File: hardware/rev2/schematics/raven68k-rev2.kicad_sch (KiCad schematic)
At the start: 16 parts, among them J1 CPLD_JTAG, SW1 RESET_SW, U1 MCP100-465D, U2 68010D, U3 XC9572XL-TQ100, X1 CLOCK

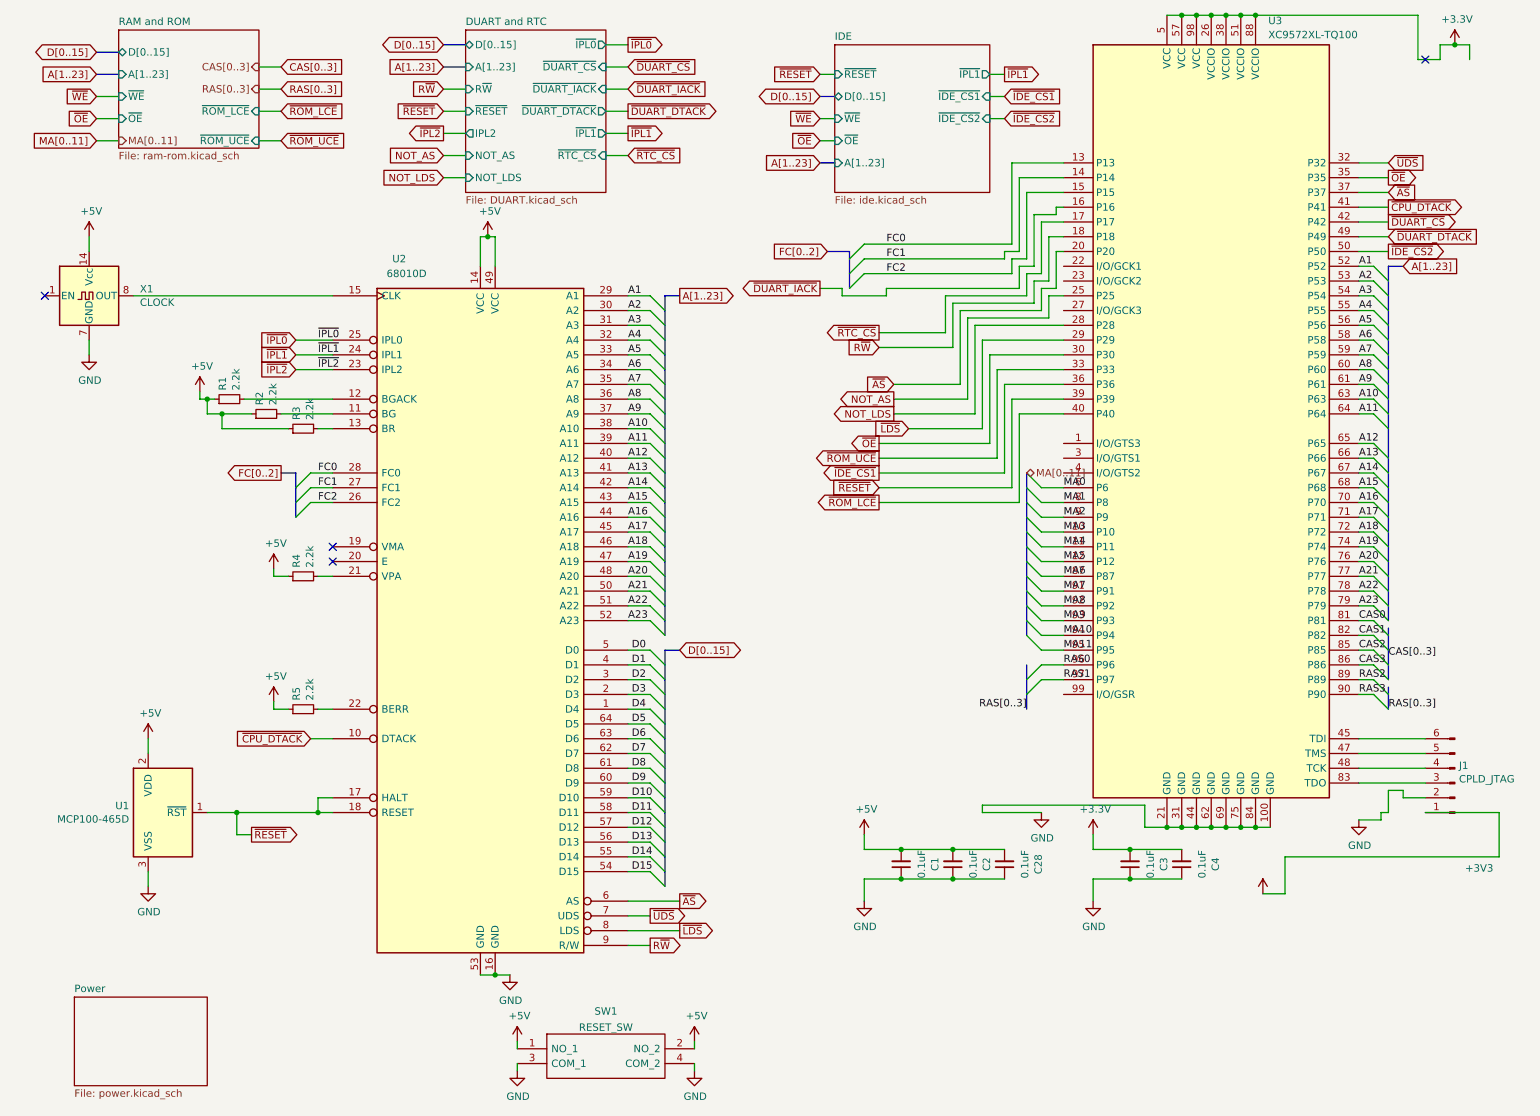
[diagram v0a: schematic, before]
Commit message: Minor adjustment to add the CLK signal to the CPLD that was forgotten. Re-did the PCB to reflect this change and also edited the component placement a bit.
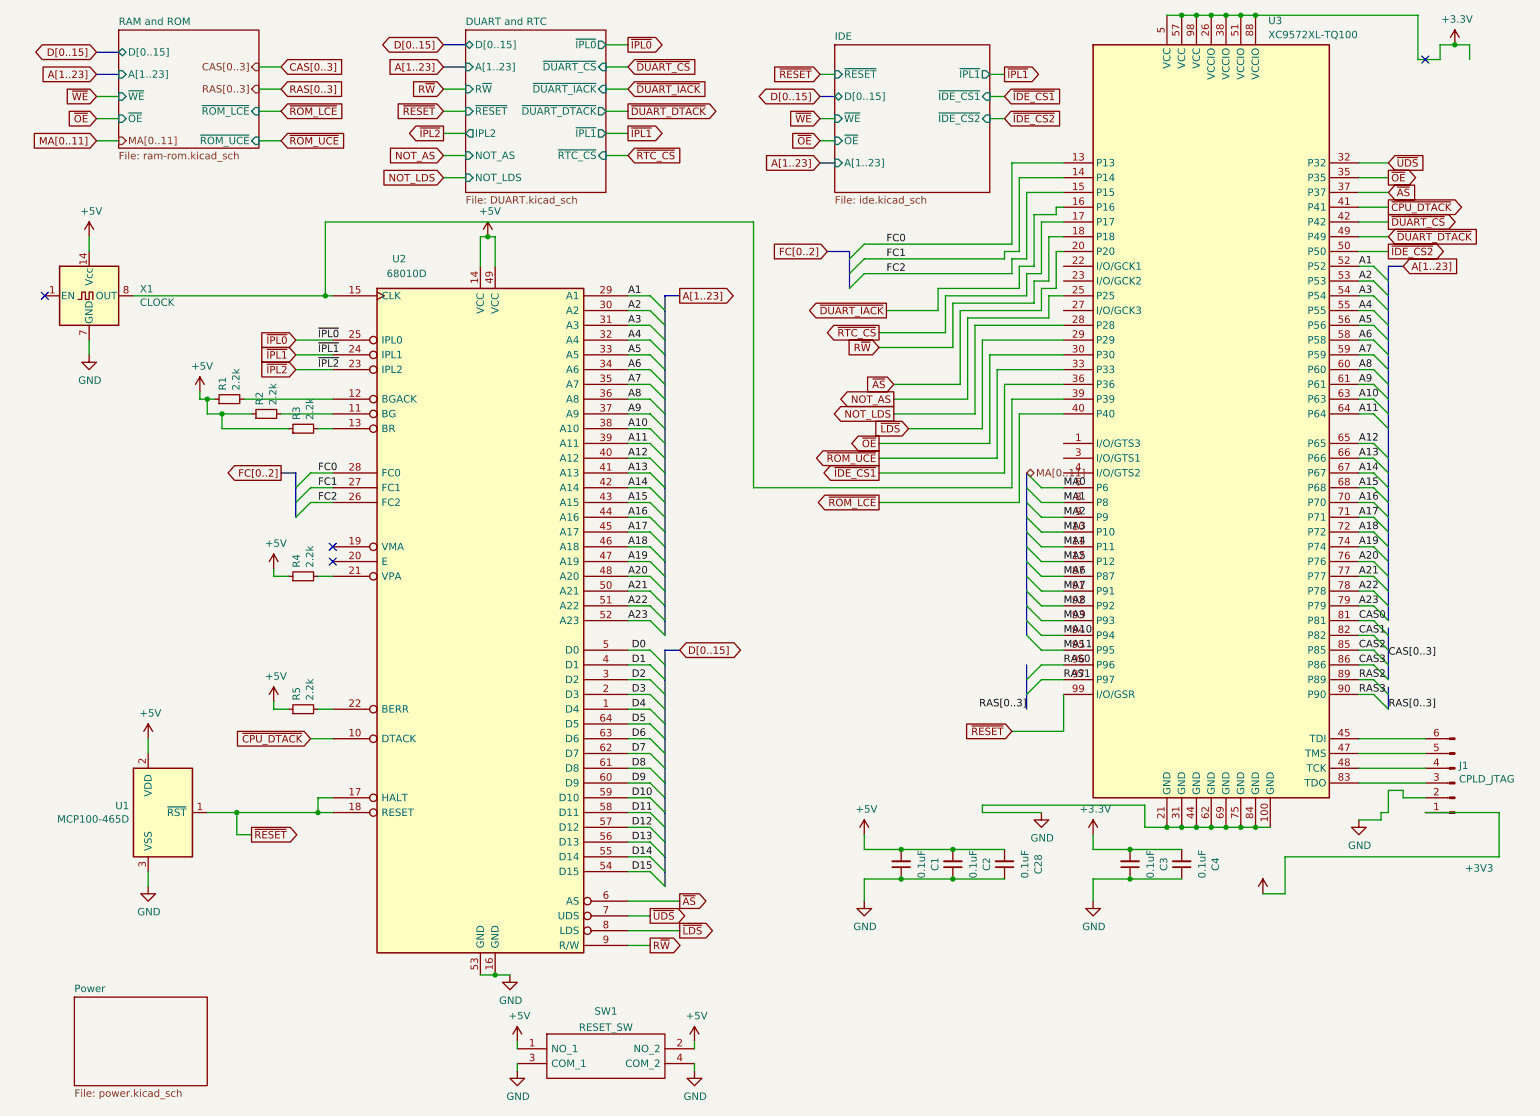
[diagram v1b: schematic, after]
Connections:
- net ~{RESET}: now also U3.99 (I/O/GSR); no longer U3.39 (P39)
- net at U2.15 (CLK), X1.8 (OUT): now also U3.39 (P39)

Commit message: ERC fixes, part 1
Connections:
- no-connect marks 4 -> 10

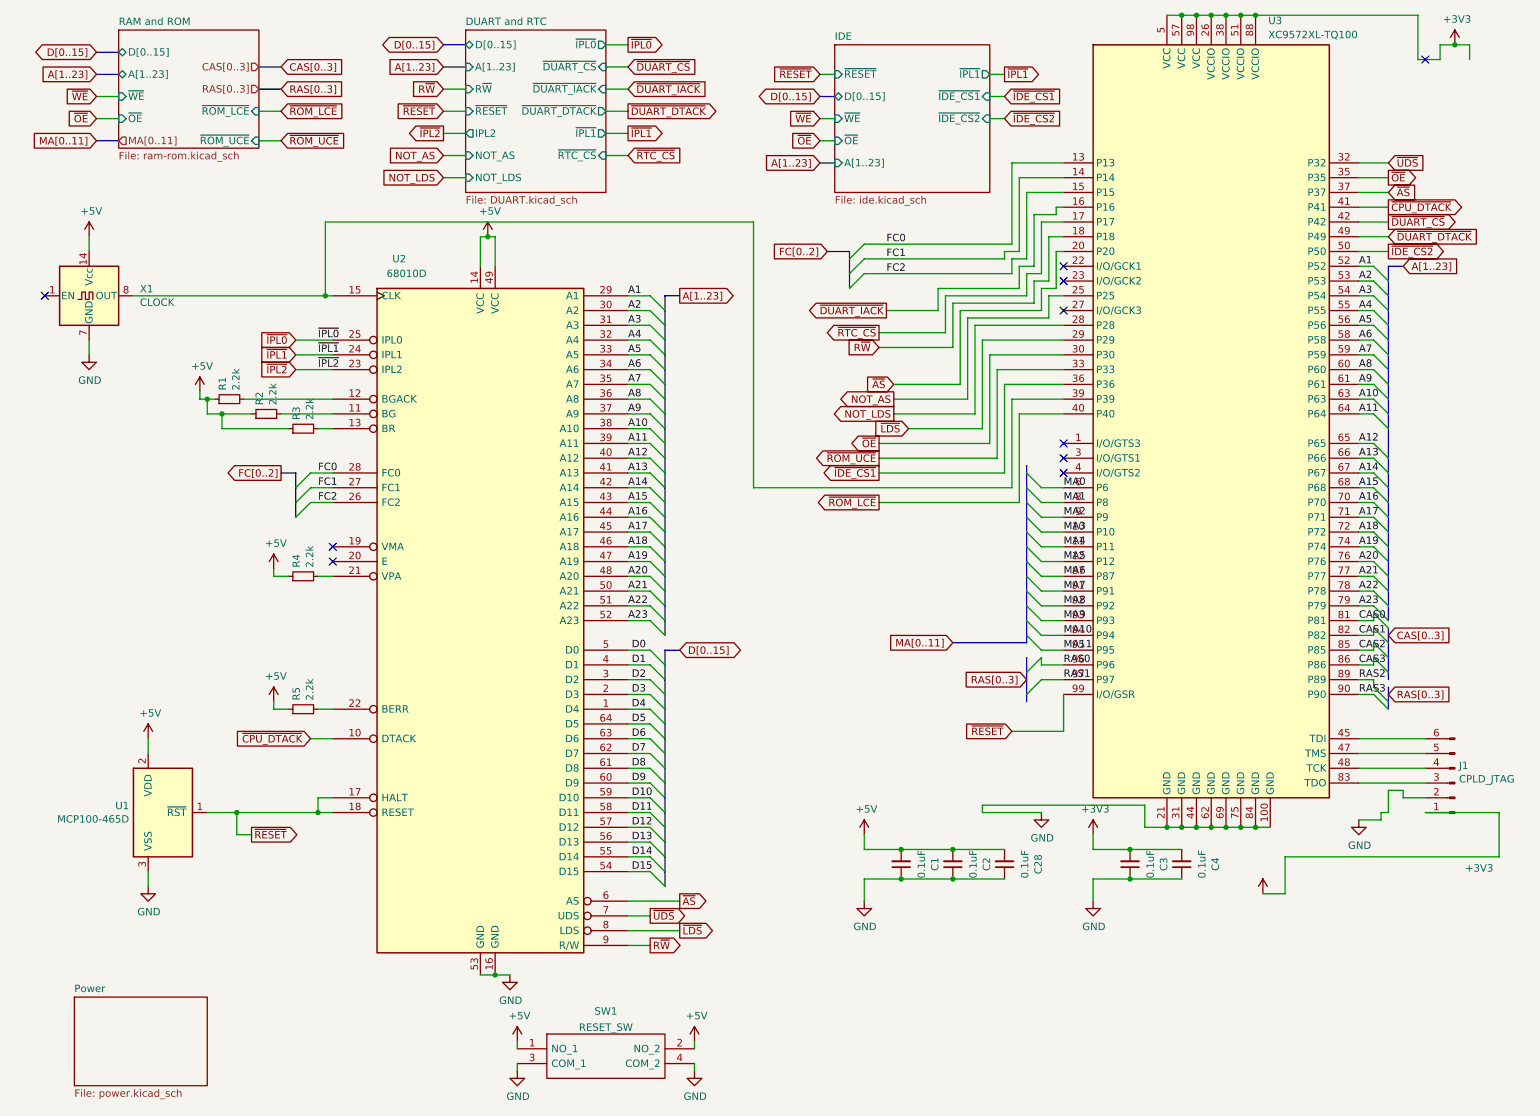
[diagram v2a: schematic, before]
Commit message: ERC fixes part 2. No more errors reported. Re-routed the PCB.
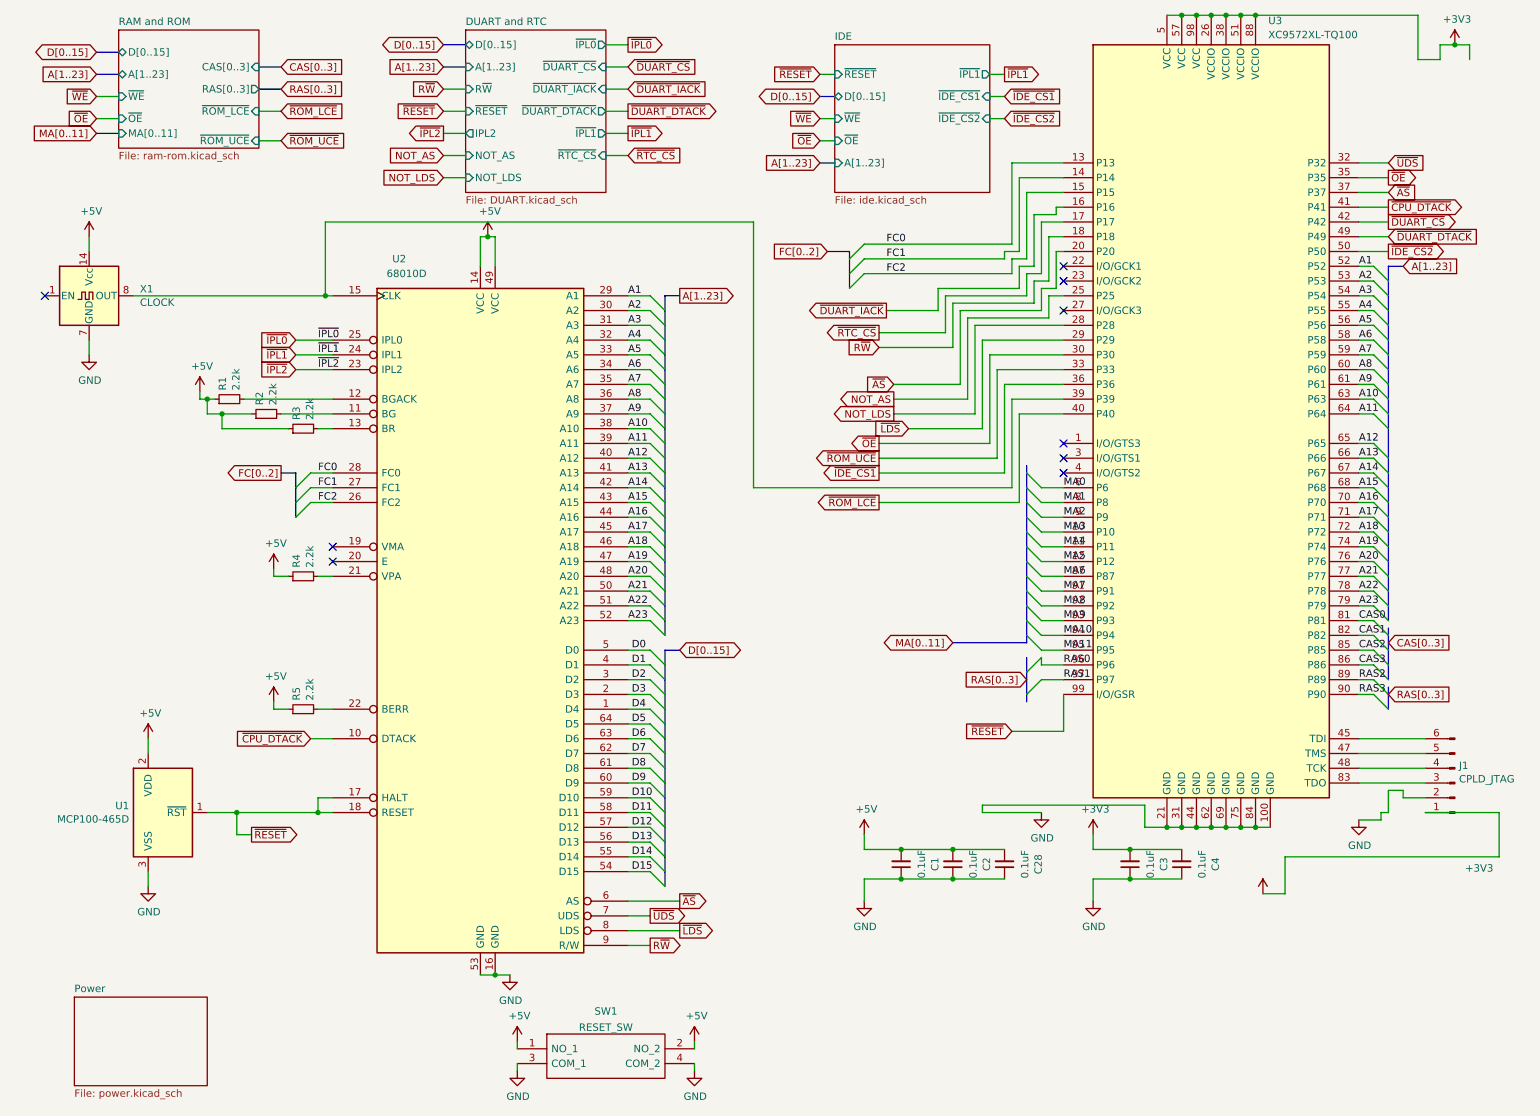
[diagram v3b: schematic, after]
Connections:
- no-connect marks 10 -> 9
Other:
- sheet RAM and ROM ports: added CAS[0..3], MA[0..11], RAS[0..3]; removed none
